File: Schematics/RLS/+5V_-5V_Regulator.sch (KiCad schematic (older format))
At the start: 12 parts, among them U2 LM317T, U3 LM337T

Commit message: Lots of changes
Completed Schematic
1/3 Done PCB
Multisim file for testing ADC protection and buffer circuit
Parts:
- R26, R27: footprint Potentiometers:Potentiometer_Trimmer_Bourns_3296Y -> Potentiometers:Potentiometer_Trimmer_Bourns_3266Y
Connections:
- net -ADJ: now reaches C42.2, R27.2, R28.1, U3.1 (ADJ)
- net +ADJ: now reaches C41.1, R25.2, R26.2, U2.1 (ADJ)
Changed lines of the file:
@@
 LIBS:valves
 LIBS:arduino_shield
-LIBS:arduino_shieldsNCL
+LIBS:RA30421051
+LIBS:RB496EATR
+LIBS:Daughterboard_Connector
 LIBS:RLS-cache
 EELAYER 25 0
@@
 F 0 "R26" V 5325 2400 50  0000 C CNN
 F 1 "1K_POT" V 5400 2400 50  0000 C CNN
-F 2 "Potentiometers:Potentiometer_Trimmer_Bourns_3296Y" H 5500 2400 50  0001 C CNN
+F 2 "Potentiometers:Potentiometer_Trimmer_Bourns_3266Y" H 5500 2400 50  0001 C CNN
 F 3 "" H 5500 2400 50  0001 C CNN
 	1    5500 2400
@@
 F 0 "R27" V 5325 3000 50  0000 C CNN
 F 1 "1K_POT" V 5400 3000 50  0000 C CNN
-F 2 "Potentiometers:Potentiometer_Trimmer_Bourns_3296Y" H 5500 3000 50  0001 C CNN
+F 2 "Potentiometers:Potentiometer_Trimmer_Bourns_3266Y" H 5500 3000 50  0001 C CNN
 F 3 "" H 5500 3000 50  0001 C CNN
 	1    5500 3000
@@
 NoConn ~ 5500 3150
 NoConn ~ 5500 2250
+Text Label 4900 3250 0    60   ~ 0
+-ADJ
+Text Label 4900 2200 0    60   ~ 0
++ADJ
 $EndSCHEMATC

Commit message: Continued PCB and Final Schematic
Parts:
- C39, C40: footprint Capacitors_SMD:C_0603_HandSoldering -> Capacitors_SMD:C_1206_HandSoldering
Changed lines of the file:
@@
 F 0 "C39" H 4325 2250 50  0000 L CNN
 F 1 "0.1uF" H 4325 2050 50  0000 L CNN
-F 2 "Capacitors_SMD:C_0603_HandSoldering" H 4338 2000 50  0001 C CNN
+F 2 "Capacitors_SMD:C_1206_HandSoldering" H 4338 2000 50  0001 C CNN
 F 3 "" H 4300 2150 50  0001 C CNN
 	1    4300 2150
@@
 F 0 "C40" H 4325 3350 50  0000 L CNN
 F 1 "0.1uF" H 4325 3150 50  0000 L CNN
-F 2 "Capacitors_SMD:C_0603_HandSoldering" H 4338 3100 50  0001 C CNN
+F 2 "Capacitors_SMD:C_1206_HandSoldering" H 4338 3100 50  0001 C CNN
 F 3 "" H 4300 3250 50  0001 C CNN
 	1    4300 3250

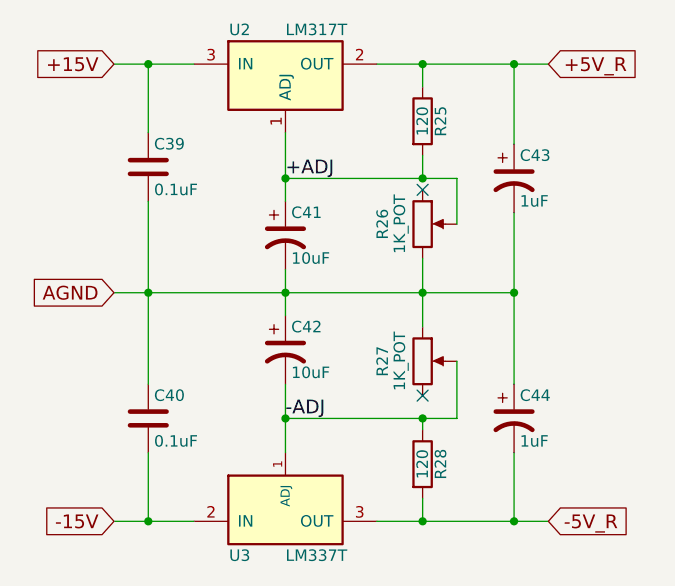
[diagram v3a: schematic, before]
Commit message: Finished PCB but...
Somehow managed to break the schematic file. I know how to fix it, but it is tedious and pointless for now (one has to go through every single individual component and verify that it is the same in the PCB, since the annotation script fucked everything up in the schematic, and therefore any new Netlist).
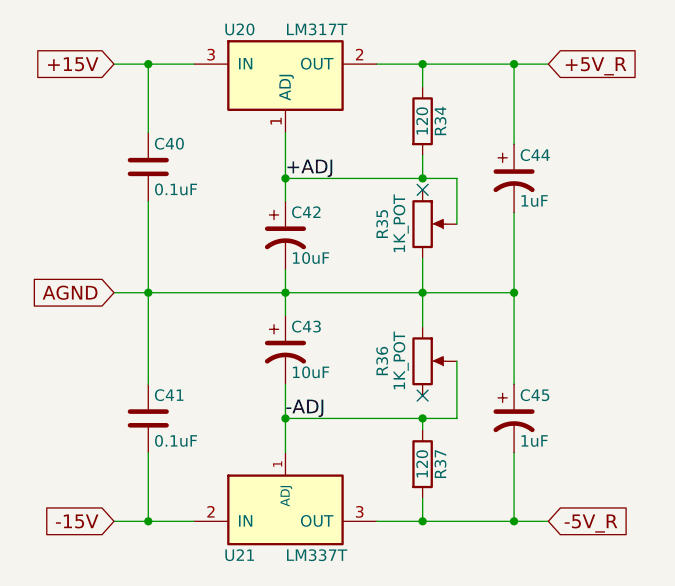
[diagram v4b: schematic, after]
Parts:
- renumbered C39 to C40, C40 to C41, C41 to C42, C42 to C43, C43 to C44, C44 to C45, R25 to R34, R26 to R35, R27 to R36, R28 to R37, U2 to U20, U3 to U21
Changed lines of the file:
@@
 $EndDescr
 $Comp
-L LM337T U3
+L LM337T U21
 U 1 1 595958FD
 P 4900 3650
-AR Path="/5959581C/595958FD" Ref="U3"  Part="1"
-AR Path="/595AEFB9/595958FD" Ref="U13"  Part="1"
-F 0 "U3" H 4700 3450 50  0000 C CNN
+F 0 "U21" H 4700 3450 50  0000 C CNN
 F 1 "LM337T" H 4900 3450 50  0000 L CNN
 F 2 "TO_SOT_Packages_THT:TO-220_Vertical" H 4900 3550 50  0001 C CIN
@@
 $EndComp
 $Comp
-L LM317T U2
+L LM317T U20
 U 1 1 59595954
 P 4900 1750
-AR Path="/5959581C/59595954" Ref="U2"  Part="1"
-AR Path="/595AEFB9/59595954" Ref="U12"  Part="1"
-F 0 "U2" H 4700 1950 50  0000 C CNN
+F 0 "U20" H 4700 1950 50  0000 C CNN
 F 1 "LM317T" H 4900 1950 50  0000 L CNN
 F 2 "TO_SOT_Packages_THT:TO-220_Vertical" H 4900 1850 50  0001 C CIN
@@
 $EndComp
 $Comp
-L CP1 C41
+L CP1 C42
 U 1 1 59596610
 P 4900 2450
-AR Path="/5959581C/59596610" Ref="C41"  Part="1"
-AR Path="/595AEFB9/59596610" Ref="C41"  Part="1"
-F 0 "C41" H 4925 2550 50  0000 L CNN
+F 0 "C42" H 4925 2550 50  0000 L CNN
 F 1 "10uF" H 4925 2350 50  0000 L CNN
 F 2 "Capacitors_SMD:CP_Elec_4x5.3" H 4900 2450 50  0001 C CNN
@@
 $EndComp
 $Comp
-L C C39
+L C C40
 U 1 1 59596655
 P 4300 2150
-AR Path="/5959581C/59596655" Ref="C39"  Part="1"
-AR Path="/595AEFB9/59596655" Ref="C39"  Part="1"
-F 0 "C39" H 4325 2250 50  0000 L CNN
+F 0 "C40" H 4325 2250 50  0000 L CNN
 F 1 "0.1uF" H 4325 2050 50  0000 L CNN
 F 2 "Capacitors_SMD:C_1206_HandSoldering" H 4338 2000 50  0001 C CNN
@@
 $EndComp
 $Comp
-L R R25
+L R R34
 U 1 1 59596672
 P 5500 1950
-AR Path="/5959581C/59596672" Ref="R25"  Part="1"
-AR Path="/595AEFB9/59596672" Ref="R25"  Part="1"
-F 0 "R25" V 5580 1950 50  0000 C CNN
+F 0 "R34" V 5580 1950 50  0000 C CNN
 F 1 "120" V 5500 1950 50  0000 C CNN
 F 2 "Resistors_SMD:R_1206_HandSoldering" V 5430 1950 50  0001 C CNN
@@
 $EndComp
 $Comp
-L C C40
+L C C41
 U 1 1 59596B6C
 P 4300 3250
-AR Path="/5959581C/59596B6C" Ref="C40"  Part="1"
-AR Path="/595AEFB9/59596B6C" Ref="C40"  Part="1"
-F 0 "C40" H 4325 3350 50  0000 L CNN
+F 0 "C41" H 4325 3350 50  0000 L CNN
 F 1 "0.1uF" H 4325 3150 50  0000 L CNN
 F 2 "Capacitors_SMD:C_1206_HandSoldering" H 4338 3100 50  0001 C CNN
@@
 AGND
 $Comp
-L CP1 C42
+L CP1 C43
 U 1 1 59597317
 P 4900 2950
-AR Path="/5959581C/59597317" Ref="C42"  Part="1"
-AR Path="/595AEFB9/59597317" Ref="C42"  Part="1"
-F 0 "C42" H 4925 3050 50  0000 L CNN
+F 0 "C43" H 4925 3050 50  0000 L CNN
 F 1 "10uF" H 4925 2850 50  0000 L CNN
 F 2 "Capacitors_SMD:CP_Elec_4x5.3" H 4900 2950 50  0001 C CNN
@@
 	4900 3100 4900 3400
 $Comp
-L R R28
+L R R37
 U 1 1 59597526
 P 5500 3450
-AR Path="/5959581C/59597526" Ref="R28"  Part="1"
-AR Path="/595AEFB9/59597526" Ref="R28"  Part="1"
-F 0 "R28" V 5580 3450 50  0000 C CNN
+F 0 "R37" V 5580 3450 50  0000 C CNN
 F 1 "120" V 5500 3450 50  0000 C CNN
 F 2 "Resistors_SMD:R_1206_HandSoldering" V 5430 3450 50  0001 C CNN
@@
 Connection ~ 5500 3250
 $Comp
-L CP1 C43
+L CP1 C44
 U 1 1 59597677
 P 5900 2200
-AR Path="/5959581C/59597677" Ref="C43"  Part="1"
-AR Path="/595AEFB9/59597677" Ref="C43"  Part="1"
-F 0 "C43" H 5925 2300 50  0000 L CNN
+F 0 "C44" H 5925 2300 50  0000 L CNN
 F 1 "1uF" H 5925 2100 50  0000 L CNN
 F 2 "Capacitors_SMD:CP_Elec_4x5.3" H 5900 2200 50  0001 C CNN
@@
 $EndComp
 $Comp
-L CP1 C44
+L CP1 C45
 U 1 1 595976C7
 P 5900 3250
-AR Path="/5959581C/595976C7" Ref="C44"  Part="1"
-AR Path="/595AEFB9/595976C7" Ref="C44"  Part="1"
-F 0 "C44" H 5925 3350 50  0000 L CNN
+F 0 "C45" H 5925 3350 50  0000 L CNN
 F 1 "1uF" H 5925 3150 50  0000 L CNN
 F 2 "Capacitors_SMD:CP_Elec_4x5.3" H 5900 3250 50  0001 C CNN
@@
 +15V
 $Comp
-L POT R26
+L POT R35
 U 1 1 595AB1DA
 P 5500 2400
-F 0 "R26" V 5325 2400 50  0000 C CNN
+F 0 "R35" V 5325 2400 50  0000 C CNN
 F 1 "1K_POT" V 5400 2400 50  0000 C CNN
 F 2 "Potentiometers:Potentiometer_Trimmer_Bourns_3266Y" H 5500 2400 50  0001 C CNN
@@
 $EndComp
 $Comp
-L POT R27
+L POT R36
 U 1 1 595AB23B
 P 5500 3000
-F 0 "R27" V 5325 3000 50  0000 C CNN
+F 0 "R36" V 5325 3000 50  0000 C CNN
 F 1 "1K_POT" V 5400 3000 50  0000 C CNN
 F 2 "Potentiometers:Potentiometer_Trimmer_Bourns_3266Y" H 5500 3000 50  0001 C CNN

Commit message: Added Things and Fixed Schematic
Added pots to schematic and pcb for adc balancing.
Fixed the component annotation and netlist in the pcb.
Shrunk the pcb down a bit.
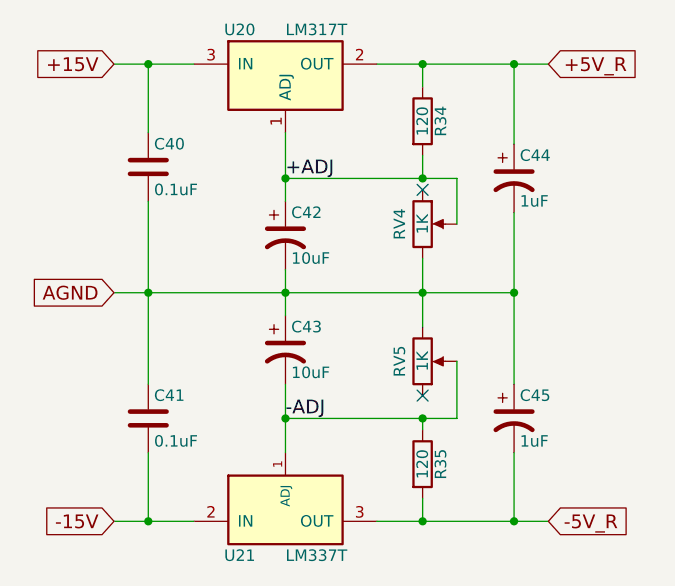
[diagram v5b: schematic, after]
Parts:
- RV4: renamed from R35; value 1K_POT -> 1K; footprint Potentiometers:Potentiometer_Trimmer_Bourns_3266Y -> RLS_CustomFootprints:Potentiometer_Trimmer_Bourns_PVG5A
- RV5: renamed from R36; value 1K_POT -> 1K; footprint Potentiometers:Potentiometer_Trimmer_Bourns_3266Y -> RLS_CustomFootprints:Potentiometer_Trimmer_Bourns_PVG5A
- renumbered R37 to R35
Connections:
- net AGND: now also RV5.3; no longer RV5.1
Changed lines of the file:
@@
 	4900 3100 4900 3400
 $Comp
-L R R37
+L R R35
 U 1 1 59597526
 P 5500 3450
-F 0 "R37" V 5580 3450 50  0000 C CNN
+F 0 "R35" V 5580 3450 50  0000 C CNN
 F 1 "120" V 5500 3450 50  0000 C CNN
 F 2 "Resistors_SMD:R_1206_HandSoldering" V 5430 3450 50  0001 C CNN
@@
 +15V
 $Comp
-L POT R35
+L POT RV4
 U 1 1 595AB1DA
 P 5500 2400
-F 0 "R35" V 5325 2400 50  0000 C CNN
-F 1 "1K_POT" V 5400 2400 50  0000 C CNN
-F 2 "Potentiometers:Potentiometer_Trimmer_Bourns_3266Y" H 5500 2400 50  0001 C CNN
+F 0 "RV4" V 5400 2400 50  0000 C CNN
+F 1 "1K" V 5500 2400 50  0000 C CNN
+F 2 "RLS_CustomFootprints:Potentiometer_Trimmer_Bourns_PVG5A" H 5500 2400 50  0001 C CNN
 F 3 "" H 5500 2400 50  0001 C CNN
 	1    5500 2400
@@
 $EndComp
 $Comp
-L POT R36
+L POT RV5
 U 1 1 595AB23B
 P 5500 3000
-F 0 "R36" V 5325 3000 50  0000 C CNN
-F 1 "1K_POT" V 5400 3000 50  0000 C CNN
-F 2 "Potentiometers:Potentiometer_Trimmer_Bourns_3266Y" H 5500 3000 50  0001 C CNN
+F 0 "RV5" V 5400 3000 50  0000 C CNN
+F 1 "1K" V 5500 3000 50  0000 C CNN
+F 2 "RLS_CustomFootprints:Potentiometer_Trimmer_Bourns_PVG5A" H 5500 3000 50  0001 C CNN
 F 3 "" H 5500 3000 50  0001 C CNN
 	1    5500 3000
-	1    0    0    -1
+	1    0    0    1
 $EndComp
 Wire Wire Line
